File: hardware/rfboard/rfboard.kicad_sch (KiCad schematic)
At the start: 19 parts, among them J1 10118194-0001LF, P2 CONN_01X03, P3 CONN_01X04, U1 SAMD21E18, U2 RFM69CW-915MHZ, U3 MIC5504-3.3YM5-T5, U4 74LVC1G125

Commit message: rfboard v2.0: schematic updates
Change-Id: Iba3a316f36017c1870a50a60d05db53b9f37ae51
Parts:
- removed C1, C2: 1uF, Capacitor_SMD:C_0603_1608Metric, symbol rfboard-rescue:C
- removed C3: 10uF, Capacitor_SMD:C_0805_2012Metric, symbol rfboard-rescue:C
- removed D1: WS2812B, homebrew:WS2812B, symbol rfboard-rescue:WS2812B-RESCUE-rfboard
- removed P3: CONN_01X04, Connector_PinHeader_2.54mm:PinHeader_1x04_P2.54mm_Vertical, symbol rfboard-rescue:CONN_01X04
- removed S1: MOMENTARY-SWITCH-SPST-SMD-4.6X2.8MM, Sparkfun-Switches:TACTILE_SWITCH_SMD_4.6X2.8MM, symbol SparkFun-Switches:MOMENTARY-SWITCH-SPST-SMD-4.6X2.8MM
- removed U1: SAMD21E18, Sparkfun-Silicon-Standard:TQFP32-08, symbol Homebrew:SAMD21E18
- removed U3: MIC5504-3.3YM5-T5, MIC5504-3.3YM5-T5:SOT23-5P95_280X145XL45X37N, symbol MIC5504-3.3YM5-T5:MIC5504-3.3YM5-T5
- removed U4: 74LVC1G125, Package_TO_SOT_SMD:SOT-353_SC-70-5, symbol rfboard-rescue:74LVC1G125
- added C1, C11, C13, C16, C18, C2, C3, C8: 100nF, Capacitor_SMD:C_0402_1005Metric, symbol Device:C
- added C10, C15, C19: 47uF, Capacitor_SMD:C_1206_3216Metric, symbol Device:C
- added C12, C14, C17, C20, C6, C9: 10uF, Capacitor_SMD:C_0603_1608Metric, symbol Device:C
- added D3: SRV05-4-P-T7, Package_TO_SOT_SMD:SOT-23-6, symbol Homebrew:SRV05-4-P-T7
- added J2: Conn_01x04, symbol Connector_Generic:Conn_01x04
- added R1: 4k7, Resistor_SMD:R_0402_1005Metric, symbol Device:R
- added R3: 22k, Resistor_SMD:R_0402_1005Metric, symbol Device:R
- added R4: 1k, Resistor_SMD:R_0402_1005Metric, symbol Device:R
- added R5, R6: 470, Resistor_SMD:R_0402_1005Metric, symbol Device:R
- added SW1: SW_Push, Homebrew:SW_TACTILE_5.1MM_TS-1187A-C-D-B, symbol Switch:SW_Push
- added U1: STM32G070KBTx, Package_QFP:LQFP-32_7x7mm_P0.8mm, symbol MCU_ST_STM32G0:STM32G070KBTx
- added U3: CH340X, Package_SO:MSOP-10_3x3mm_P0.5mm, symbol Interface_USB:CH340X
- added U4: XL-0807RGBC-WS2812B, easyeda2kicad:LED-SMD_4P-L2.0-W1.8_CY-0807, symbol Homebrew:XL-0807RGBC-WS2812B
- added U5: XC6206P332MR-G, Package_TO_SOT_SMD:SOT-23-3, symbol Regulator_Linear:XC6206PxxxMR
- C4, C5: value 1uF -> 100nF; footprint Capacitor_SMD:C_0603_1608Metric -> Capacitor_SMD:C_0402_1005Metric; LCSC (none) -> C307331
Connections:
- net +3V3: now also C13.1, C14.1, C15.1, C20.1, C6.1, J2.1 (Pin_1), U1.4 (VDD), U5.2 (VO)
- net +5V: now also C1.1, C10.1, C11.1, C12.1, C16.1, C17.1, C18.1, C19.1, C3.1, C9.1, D3.5 (REF), U3.7 (VCC), U4.1 (VDD), U5.3 (VI)
- net GND: now also C1.2, C10.2, C11.2, C12.2, C13.2, C14.2, C15.2, C16.2, C17.2, C18.2, C19.2, C2.2, C20.2, C3.2, C6.2, C9.2, D3.2 (GND), J2.2 (Pin_2), R1.2, SW1.1, U1.5 (VSS), U3.3 (GND), U4.3 (GND), U5.1 (GND)
- net LED_EXTERNAL: now also D3.4 (IO3), R5.2
- net LED_INTERNAL: now also R6.1
- net USB_D+ renamed USB_DP
- net USB_DP: now also D3.1 (IO1), U3.1 (UD+)
- net USB_D- renamed USB_DN
- net USB_DN: now also D3.3 (IO2), U3.2 (UD-)
- new net: R5.1, U4.2 (DOUT)
- new net: R6.2, U4.4 (DIN)
- new net: R4.1, SW1.2
- new net: C8.2, R4.2, U1.6 (NRST)
- new net: C2.1, U3.10 (V3)
- new net: R1.1, R3.1, U3.6 (TNOW/~{DTR})
- new net BOOT0: J2.4 (Pin_4), R3.2, U1.25 (PA14)
- new net SWDIO: J2.3 (Pin_3), U1.24 (PA13)
- new net USART_RX: U3.8 (TXD)
- new net USART_TX: U3.9 (RXD)
- new net ~{RTS}: C8.1, U3.4 (~{RTS})
- no-connect marks 22 -> 7
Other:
- note added: ""One-click USB download of MCU" configuration"
- note added: "5V -> 3.3V LDO"
- note added: "BOOT0 == SWCLK"
- note added: "Offboard LED"
- note added: "Onboard LED"
- note added: "SWD header"
- note added: "USB to serial"
- note removed: "1"
- note removed: "2018-01-08"
- note removed: "ARM Serial Wire Debug"
- note removed: "Off board LED"
- moved on the sheet: C7, D2, J1, L1, P2, R2, U2

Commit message: First pass at schematic
Change-Id: Iee9cb97348f849087d02872423449673015ce7d3
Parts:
- removed D2: LED, LED_SMD:LED_0603_1608Metric, symbol rfboard-rescue:LED
- added C21, C22, C23, C25: 100nF, Capacitor_SMD:C_0402_1005Metric, symbol Device:C
- added C24: 47pF, Capacitor_SMD:C_0402_1005Metric, symbol Device:C
- added D1, D4, D5, D6: ESD5Z5.0, Diode_SMD:D_SOD-523, symbol Diode:ESD5Zxx
- added D2: RED, LED_SMD:LED_0603_1608Metric, symbol Device:LED
- added J3: 2337019-1, Homebrew:CONN_2337019-1, symbol Homebrew:TE_U.FL_MALE_SMT
- added JP1: SolderJumper_2_Open, Jumper:SolderJumper-2_P1.3mm_Open_TrianglePad1.0x1.5mm, symbol Jumper:SolderJumper_2_Open
- added R10, R9: 10k, Resistor_SMD:R_0402_1005Metric, symbol rfboard-rescue:R
- added R11: 15k, Resistor_SMD:R_0402_1005Metric, symbol rfboard-rescue:R
- added R7, R8: 1k, Resistor_SMD:R_0603_1608Metric, symbol rfboard-rescue:R
- added SW2, SW3: SW_Push, Homebrew:SW_TACTILE_5.1MM_TS-1187A-C-D-B, symbol Switch:SW_Push
- added U6: HX 1210-C06, easyeda2kicad:SMD-2P_L2.9-W2.4_C9900033648, symbol easyeda2kicad:HX1210-C06
- C7: footprint Capacitor_SMD:C_0603_1608Metric -> Capacitor_SMD:C_0402_1005Metric_Pad0.74x0.62mm_HandSolder; LCSC (none) -> C72134
- L1: footprint Inductor_SMD:L_0603_1608Metric -> Inductor_SMD:L_0402_1005Metric_Pad0.77x0.64mm_HandSolder; LCSC (none) -> C382409
- U4: LCSC (none) -> C3646929; LCSC Part C3646929 -> (none)
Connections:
- net +3V3: now also D4.1 (K), U6.1
- net +5V: now also R10.2
- net GND: now also C21.2, C22.2, C23.2, C24.2, C25.2, D1.2 (A), D2.1 (K), D4.2 (A), D5.2 (A), D6.2 (A), J3.2, J3.3, R11.1, R9.1, SW2.1, SW3.1
- net LED_INTERNAL: now also U1.11 (PA4)
- net RADIO_DIO0: now also U1.9 (PA2)
- net RADIO_MISO: now also U1.28 (PB4)
- net RADIO_MOSI: now also U1.29 (PB5)
- net RADIO_NSS: now also U1.26 (PA15)
- net RADIO_SCK: now also U1.27 (PB3)
- net SIMPLE_LED: now also R2.1, U1.16 (PB1); no longer R2.2
- net USART_RX: now also U1.23 (PA10/PA12)
- net USART_TX: now also U1.22 (PA9/PA11)
- net at C7.2, U2.1 (ANT): now also JP1.1 (A)
- net at C8.2, R4.2, U1.6 (NRST): now also C23.1, D6.1 (K)
- net VIBRATION_SENSOR: now reaches U1.10 (PA3)
- net VIBRATION_SENSOR: now also C24.1, R9.2, U6.2
- net SW1: now reaches U1.30 (PB6)
- net SW1: now also C21.1, D1.1 (K), R7.1
- net SW2: now reaches U1.31 (PB7)
- net SW2: now also C22.1, D5.1 (K), R8.1
- net 5V_DIVIDED: now reaches U1.7 (PA0)
- net 5V_DIVIDED: now also C25.1, R10.1, R11.2
- new net: D2.2 (A), R2.2
- new net: R8.2, SW3.2
- new net: R7.2, SW2.2
- new net ANTENNA_UFL: J3.1, JP1.2 (B)
- no-connect marks 7 -> 19
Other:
- note added: "ADC_IN0"
- note added: "SPI1"
- note added: "SPI2_MOSI"
- note added: "TIM14_CH1"
- note added: "TIM15_CH2"
- moved on the sheet: C1, C10, C11, C12, C13, C14, C15, C16, C17, C18, C19, C2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

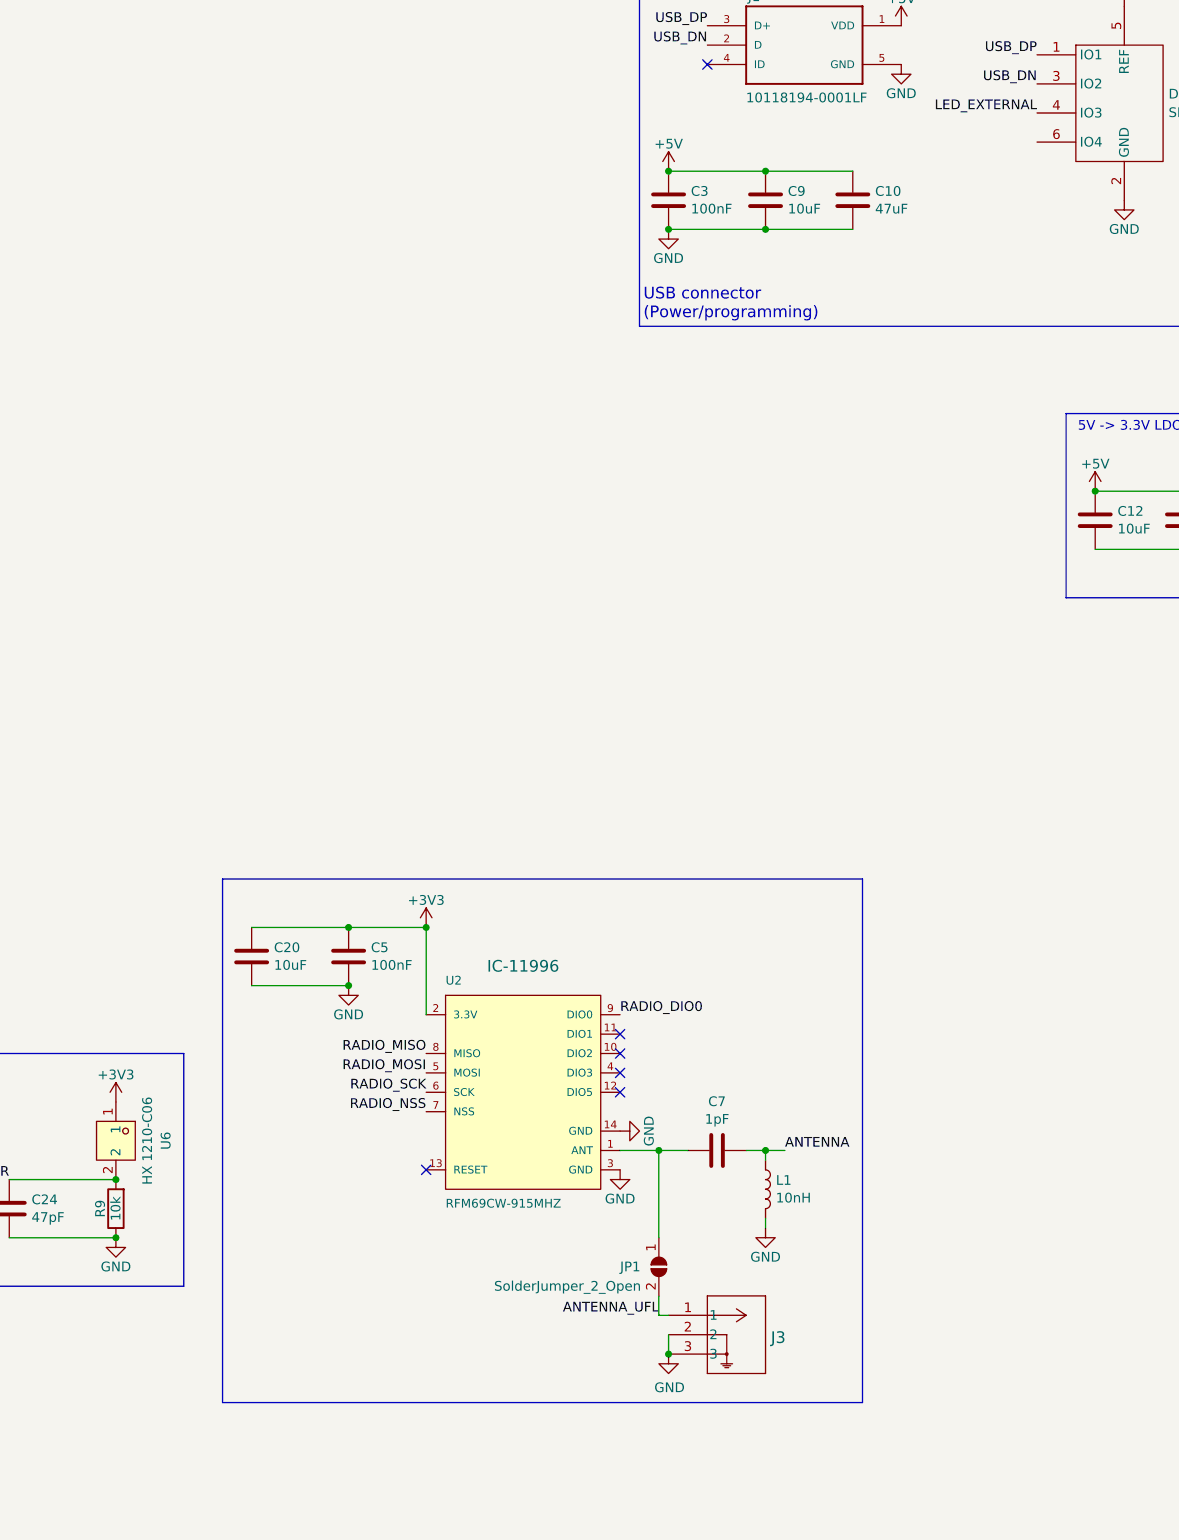
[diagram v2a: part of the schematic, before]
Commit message: rfboard: add LC filter for radio
Change-Id: I23dd460225624ee06ec1c7d5b5e8e44295342c63
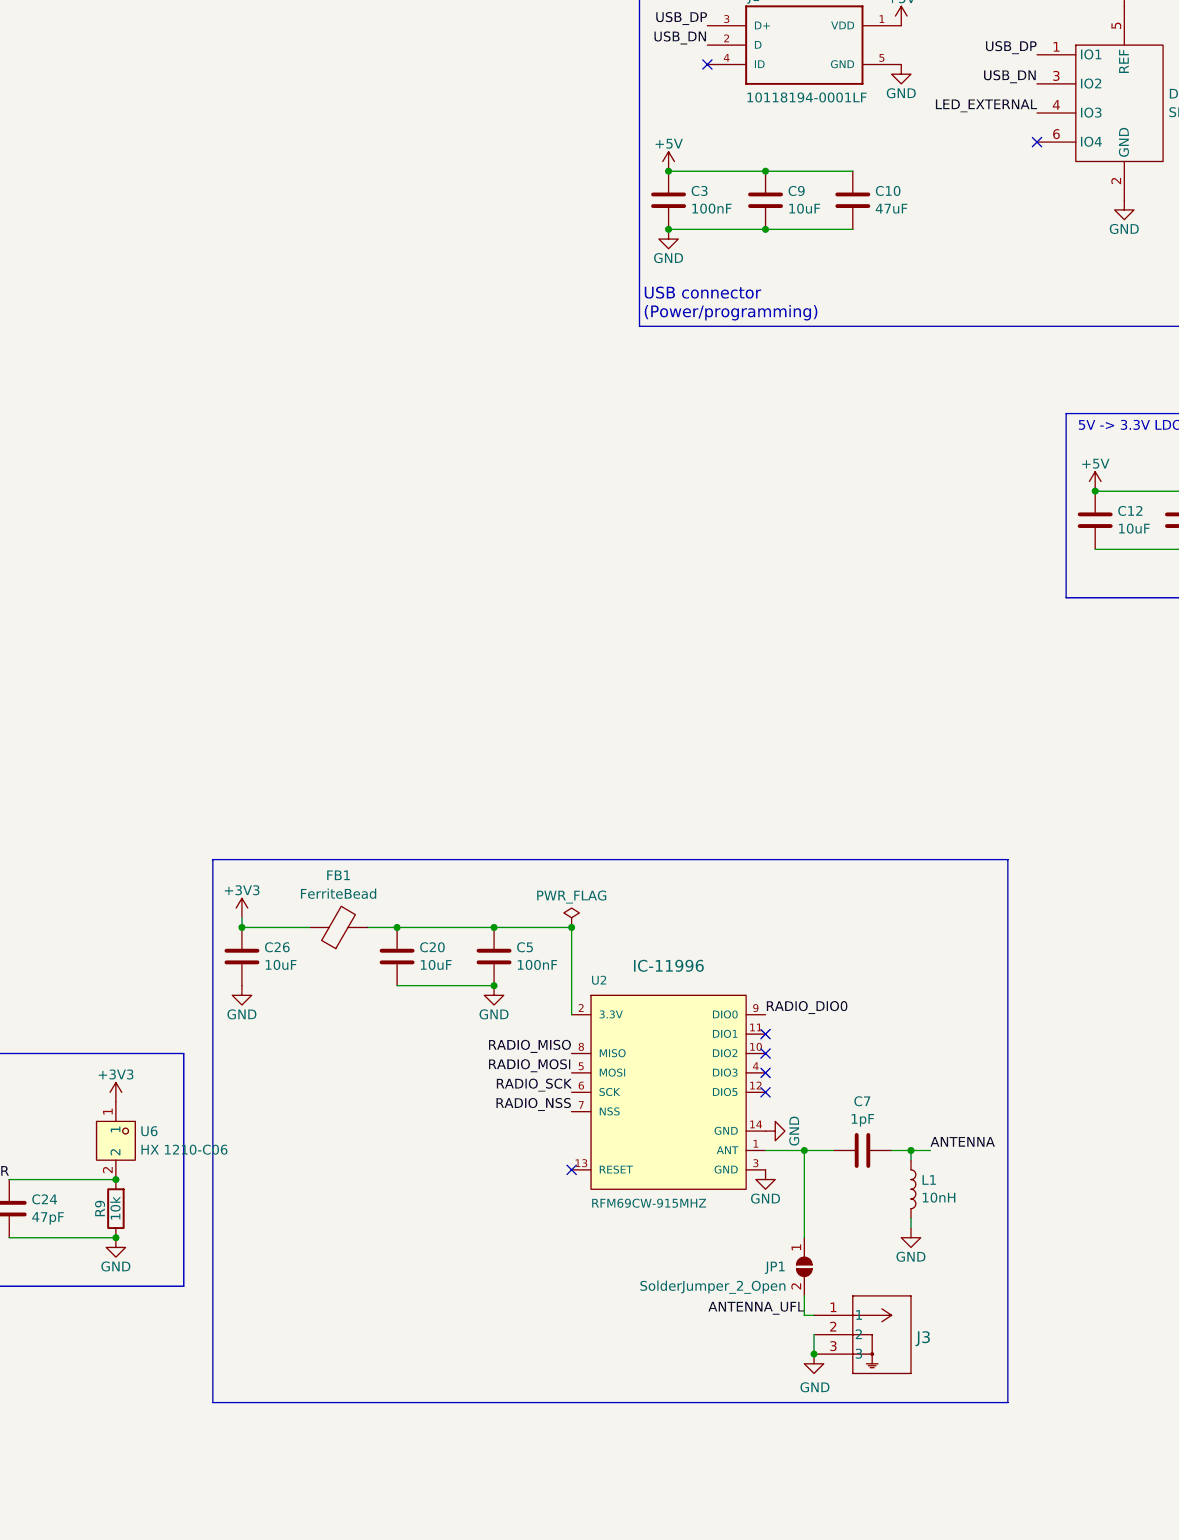
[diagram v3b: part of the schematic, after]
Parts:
- added C26: 10uF, Capacitor_SMD:C_0603_1608Metric, symbol Device:C
- added FB1: FerriteBead, Inductor_SMD:L_0603_1608Metric_Pad1.05x0.95mm_HandSolder, symbol Device:FerriteBead
- J1: footprint homebrew:FRAMATOME_10118194-0001LF_fixed_bridges -> FRAMATOME_10118194-0001LF
- U2: footprint homebrew:RFM69CW-minimalpads -> RFM69CW-XXXS2
- U6: symbol easyeda2kicad:HX1210-C06 -> Homebrew:HX1210-C06; LCSC Part (none) -> C42371120
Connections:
- net +3V3: now also C26.1, FB1.1; no longer C20.1, C5.1, U2.2 (3.3V)
- net GND: now also C26.2
- new net: C20.1, C5.1, FB1.2, U2.2 (3.3V)
- no-connect marks 19 -> 20
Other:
- moved on the sheet: C20, C5, C7, J3, JP1, L1, U2

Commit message: rfboard: first pass at component placement for v2.0
Change-Id: I4c465cc58b982850d15f3562f19207050c8a0873
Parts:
- removed U2: RFM69CW-915MHZ, RFM69CW-XXXS2, symbol SparkFun-RF:RFM69CW-915MHZ
- added U2: RFM69HCW, Homebrew:RFM69HCW-minimalpads, symbol Homebrew:RFM69HCW
- H3: footprint homebrew:3_pin_2.54mm_pitch_strain_relief -> Homebrew:3_pin_2.54mm_pitch_strain_relief; now not fitted
- J1: footprint FRAMATOME_10118194-0001LF -> Homebrew:FRAMATOME_10118194-0001LF_fixed_bridges; LCSC (none) -> C132563
- J2: footprint (none) -> Homebrew:PinHeader_1x04_P2.54mm_Vertical_NoPlastic; now not fitted
- J3, JP1, P2: now not fitted
- R11: LCSC (none) -> C25756
- R2, R7, R8: footprint Resistor_SMD:R_0603_1608Metric -> Resistor_SMD:R_0402_1005Metric; LCSC (none) -> C11702
- U1: LCSC (none) -> C529339
- U3: LCSC (none) -> C3035748
- U4: footprint easyeda2kicad:LED-SMD_4P-L2.0-W1.8_CY-0807 -> Homebrew:LED-SMD_4P-L2.0-W1.8_CY-0807
- U6: footprint easyeda2kicad:SMD-2P_L2.9-W2.4_C9900033648 -> Homebrew:SMD-2P_L2.9-W2.4_C9900033648
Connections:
- net GND: now also U2.1 (GND), U2.10 (GND), U2.8 (GND)
- net RADIO_DIO0: now also U2.14 (DIO0)
- net RADIO_MISO: now also U2.2 (MISO)
- net RADIO_MOSI: now also U2.3 (MOSI)
- net RADIO_NSS: now also U2.5 (NSS)
- net RADIO_SCK: now also U2.4 (SCK)
- net at C7.2, JP1.1 (A): now also U2.9 (ANT)
- net at C20.1, C5.1, FB1.2: now also U2.13 (3.3V)
- no-connect marks 20 -> 21
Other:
- moved on the sheet: C20, C26, C5, C7, FB1, L1

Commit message: rfboard PCB v2.0
Change-Id: Ic39936a14b05c72f947b18cbfe92ca4c5239ed35
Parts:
- added D7: ESD5Z5.0, Diode_SMD:D_SOD-523, symbol Diode:ESD5Zxx
- added J4: Conn_01x02, Homebrew:PinHeader_1x02_P2.54mm_Vertical_NoPlastic, symbol Connector_Generic:Conn_01x02
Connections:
- net +5V: now also J4.2 (Pin_2)
- net GND: now also D7.2 (A), J4.1 (Pin_1)
- net LED_EXTERNAL: now also D7.1 (K); no longer D3.4 (IO3)
- net VIBRATION_SENSOR: now also U1.18 (PA8); no longer U1.10 (PA3)
- no-connect marks 21 -> 22
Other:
- note added: "TIM1_CH1"
- note removed: "TIM15_CH2"
